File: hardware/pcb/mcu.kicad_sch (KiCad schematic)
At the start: 10 parts, among them J3 FSR402, U1 ESP32-WROOM-32E-N8R2

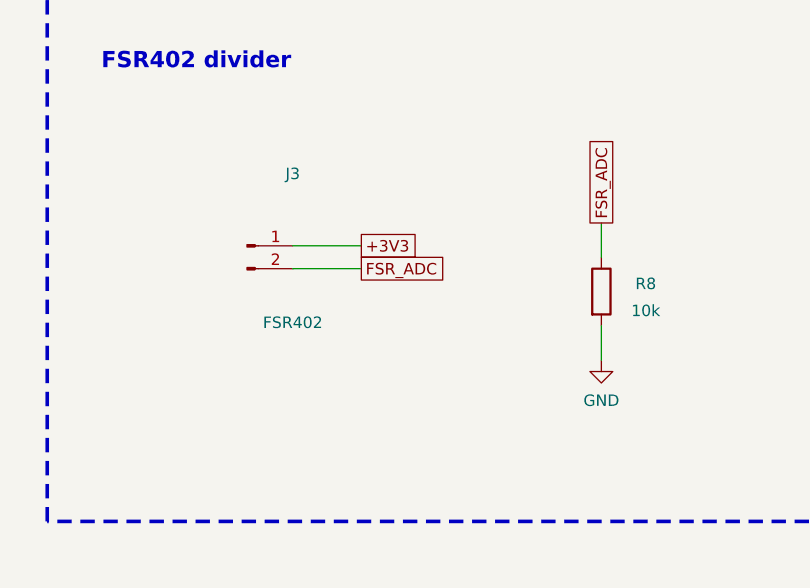
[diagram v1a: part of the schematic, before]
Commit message: Use official CAD and shrink the hw_v1 board to 37x30 mm.
Replace the hand-drawn AFE4900, AD5940, ADS1292R, AS7341, MLX90632,
TMP117, LSM6DSV80X, and MCP73831 symbols and footprints with the
SnapMagic and Ultra Librarian libraries. ADS1292R is now the QFN-32
ADS1292RIRSMT, and MLX90632SLD-DCB-100-SP moves SDA/SCL onto the
existing 1.8 V bus. Pin headers and mounting holes are flat solder
pads. The unrouted 4-layer placement keeps the antenna on the left
edge and the skin sensors together on the bottom.

Co-authored-by: Riyu-D1 <Riyu-D1@users.noreply.github.com>
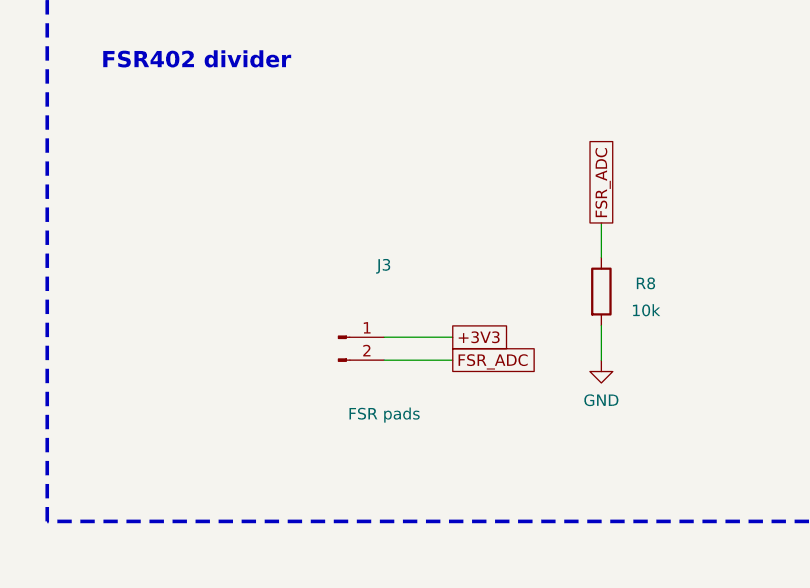
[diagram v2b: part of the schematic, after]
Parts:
- J3: value FSR402 -> FSR pads; footprint Connector_PinHeader_2.54mm:PinHeader_1x02_P2.54mm_Vertical -> vitalq:Pads_FSR
- TP1, TP2: now left out of the parts list

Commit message: Seat the QFN models and drop passives the datasheets do not require.
The ADS1292R STEP is already Z-up, so the extra X rotation stood the
4x4x1 mm body on edge. Remove TP1, TP2, C5, C12, C17, C31 and R4, add
the 1 uF AVDD bulk capacitor, and shorten the outline to 36.2 x 27.8 mm.

Co-authored-by: Riyu-D1 <Riyu-D1@users.noreply.github.com>
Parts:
- removed TP1: EN, TestPoint:TestPoint_Pad_D1.5mm, symbol vitalq:TestPoint
- removed TP2: IO0, TestPoint:TestPoint_Pad_D1.5mm, symbol vitalq:TestPoint
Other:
- note added: "EN and IO0 have pull-ups only. Download uses the module pads. There are no buttons."
- note removed: "TP1 and TP2 are pads so EN and IO0 can be strapped for download. There are no buttons."
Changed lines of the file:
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@@
 		(instances
 			(project "vitalq_hw_v1"
-				(path "/6fcf6b13-4a8e-4f25-a8b9-d34cb547168d/a5fd4a7f-7072-43f1-b967-7f2863112463"
+				(path "/1ff916b4-4a8a-459e-a757-b43de2b086a6/412652e5-da28-4ff8-bcda-4db89714720c"
 					(reference "U1")
 					(unit 1)
@@
 		(on_board no)
 		(dnp no)
-		(property "Reference" "#PWR028"
+		(property "Reference" "#PWR026"
 			(at 149.86 95.99 0)
 			(effects (font (size 1.27 1.27)) (hide yes))
@@
 		(instances
 			(project "vitalq_hw_v1"
-				(path "/6fcf6b13-4a8e-4f25-a8b9-d34cb547168d/a5fd4a7f-7072-43f1-b967-7f2863112463"
-					(reference "#PWR028")
+				(path "/1ff916b4-4a8a-459e-a757-b43de2b086a6/412652e5-da28-4ff8-bcda-4db89714720c"
+					(reference "#PWR026")
 					(unit 1)
 				)
@@
 		(on_board no)
 		(dnp no)
-		(property "Reference" "#PWR029"
+		(property "Reference" "#PWR027"
 			(at 149.86 179.81 0)
 			(effects (font (size 1.27 1.27)) (hide yes))
@@
 		(instances
 			(project "vitalq_hw_v1"
-				(path "/6fcf6b13-4a8e-4f25-a8b9-d34cb547168d/a5fd4a7f-7072-43f1-b967-7f2863112463"
-					(reference "#PWR029")
+				(path "/1ff916b4-4a8a-459e-a757-b43de2b086a6/412652e5-da28-4ff8-bcda-4db89714720c"
+					(reference "#PWR027")
 					(unit 1)
 				)
@@
 		(instances
 			(project "vitalq_hw_v1"
-				(path "/6fcf6b13-4a8e-4f25-a8b9-d34cb547168d/a5fd4a7f-7072-43f1-b967-7f2863112463"
+				(path "/1ff916b4-4a8a-459e-a757-b43de2b086a6/412652e5-da28-4ff8-bcda-4db89714720c"
 					(reference "C7")
 					(unit 1)
@@
 		(on_board no)
 		(dnp no)
-		(property "Reference" "#PWR030"
+		(property "Reference" "#PWR028"
 			(at 54.61 49.0 0)
 			(effects (font (size 1.27 1.27)) (hide yes))
@@
 		(instances
 			(project "vitalq_hw_v1"
-				(path "/6fcf6b13-4a8e-4f25-a8b9-d34cb547168d/a5fd4a7f-7072-43f1-b967-7f2863112463"
-					(reference "#PWR030")
+				(path "/1ff916b4-4a8a-459e-a757-b43de2b086a6/412652e5-da28-4ff8-bcda-4db89714720c"
+					(reference "#PWR028")
 					(unit 1)
 				)
@@
 		(on_board no)
 		(dnp no)
-		(property "Reference" "#PWR031"
+		(property "Reference" "#PWR029"
 			(at 54.61 64.24 0)
 			(effects (font (size 1.27 1.27)) (hide yes))
@@
 		(instances
 			(project "vitalq_hw_v1"
-				(path "/6fcf6b13-4a8e-4f25-a8b9-d34cb547168d/a5fd4a7f-7072-43f1-b967-7f2863112463"
-					(reference "#PWR031")
+				(path "/1ff916b4-4a8a-459e-a757-b43de2b086a6/412652e5-da28-4ff8-bcda-4db89714720c"
+					(reference "#PWR029")
 					(unit 1)
 				)
@@
 		(instances
 			(project "vitalq_hw_v1"
-				(path "/6fcf6b13-4a8e-4f25-a8b9-d34cb547168d/a5fd4a7f-7072-43f1-b967-7f2863112463"
+				(path "/1ff916b4-4a8a-459e-a757-b43de2b086a6/412652e5-da28-4ff8-bcda-4db89714720c"
 					(reference "C8")
 					(unit 1)
@@
 		(on_board no)
 		(dnp no)
-		(property "Reference" "#PWR032"
+		(property "Reference" "#PWR030"
 			(at 77.47 49.0 0)
 			(effects (font (size 1.27 1.27)) (hide yes))
@@
 		(instances
 			(project "vitalq_hw_v1"
-				(path "/6fcf6b13-4a8e-4f25-a8b9-d34cb547168d/a5fd4a7f-7072-43f1-b967-7f2863112463"
-					(reference "#PWR032")
+				(path "/1ff916b4-4a8a-459e-a757-b43de2b086a6/412652e5-da28-4ff8-bcda-4db89714720c"
+					(reference "#PWR030")
 					(unit 1)
 				)
@@
 		(on_board no)
 		(dnp no)
-		(property "Reference" "#PWR033"
+		(property "Reference" "#PWR031"
 			(at 77.47 64.24 0)
 			(effects (font (size 1.27 1.27)) (hide yes))
@@
 		(instances
 			(project "vitalq_hw_v1"
-				(path "/6fcf6b13-4a8e-4f25-a8b9-d34cb547168d/a5fd4a7f-7072-43f1-b967-7f2863112463"
-					(reference "#PWR033")
+				(path "/1ff916b4-4a8a-459e-a757-b43de2b086a6/412652e5-da28-4ff8-bcda-4db89714720c"
+					(reference "#PWR031")
 					(unit 1)
 				)
@@
 		(instances
 			(project "vitalq_hw_v1"
-				(path "/6fcf6b13-4a8e-4f25-a8b9-d34cb547168d/a5fd4a7f-7072-43f1-b967-7f2863112463"
+				(path "/1ff916b4-4a8a-459e-a757-b43de2b086a6/412652e5-da28-4ff8-bcda-4db89714720c"
 					(reference "R5")
 					(unit 1)
@@
 		(on_board no)
 		(dnp no)
-		(property "Reference" "#PWR034"
+		(property "Reference" "#PWR032"
 			(at 330.2 52.81 0)
 			(effects (font (size 1.27 1.27)) (hide yes))
@@
 		(instances
 			(project "vitalq_hw_v1"
-				(path "/6fcf6b13-4a8e-4f25-a8b9-d34cb547168d/a5fd4a7f-7072-43f1-b967-7f2863112463"
-					(reference "#PWR034")
+				(path "/1ff916b4-4a8a-459e-a757-b43de2b086a6/412652e5-da28-4ff8-bcda-4db89714720c"
+					(reference "#PWR032")
 					(unit 1)
 				)
@@
 		(instances
 			(project "vitalq_hw_v1"
-				(path "/6fcf6b13-4a8e-4f25-a8b9-d34cb547168d/a5fd4a7f-7072-43f1-b967-7f2863112463"
+				(path "/1ff916b4-4a8a-459e-a757-b43de2b086a6/412652e5-da28-4ff8-bcda-4db89714720c"
 					(reference "R6")
 					(unit 1)
@@
 		(on_board no)
 		(dnp no)
-		(property "Reference" "#PWR035"
+		(property "Reference" "#PWR033"
 			(at 351.79 52.81 0)
 			(effects (font (size 1.27 1.27)) (hide yes))
@@
 		(instances
 			(project "vitalq_hw_v1"
-				(path "/6fcf6b13-4a8e-4f25-a8b9-d34cb547168d/a5fd4a7f-7072-43f1-b967-7f2863112463"
-					(reference "#PWR035")
+				(path "/1ff916b4-4a8a-459e-a757-b43de2b086a6/412652e5-da28-4ff8-bcda-4db89714720c"
+					(reference "#PWR033")
 					(unit 1)
 				)
@@
 		(instances
 			(project "vitalq_hw_v1"
-				(path "/6fcf6b13-4a8e-4f25-a8b9-d34cb547168d/a5fd4a7f-7072-43f1-b967-7f2863112463"
+				(path "/1ff916b4-4a8a-459e-a757-b43de2b086a6/412652e5-da28-4ff8-bcda-4db89714720c"
 					(reference "R7")
 					(unit 1)
@@
 		(on_board no)
 		(dnp no)
-		(property "Reference" "#PWR036"
+		(property "Reference" "#PWR034"
 			(at 373.38 52.81 0)
 			(effects (font (size 1.27 1.27)) (hide yes))
@@
 		(instances
 			(project "vitalq_hw_v1"
-				(path "/6fcf6b13-4a8e-4f25-a8b9-d34cb547168d/a5fd4a7f-7072-43f1-b967-7f2863112463"
-					(reference "#PWR036")
-					(unit 1)
-				)
-			)
-		)
-	)
-	(symbol
-		(lib_id "vitalq:TestPoint")
-		(at 330.2 77.47 0)
-		(unit 1)
-		(exclude_from_sim no)
-		(in_bom no)
-		(on_board yes)
-		(dnp no)
-		(property "Reference" "TP1"
-			(at 334.5 76.6 0)
-			(effects (font (size 1.27 1.27)))
-		)
-		(property "Value" "EN"
-			(at 334.5 79.6 0)
-			(effects (font (size 1.27 1.27)))
-		)
-		(property "Footprint" "TestPoint:TestPoint_Pad_D1.5mm"
-			(at 330.2 77.47 0)
-			(effects (font (size 1.27 1.27)) (hide yes))
-		)
-		(property "Datasheet" ""
-			(at 330.2 77.47 0)
-			(effects (font (size 1.27 1.27)) (hide yes))
-		)
-		(pin "1")
-		(instances
-			(project "vitalq_hw_v1"
-				(path "/6fcf6b13-4a8e-4f25-a8b9-d34cb547168d/a5fd4a7f-7072-43f1-b967-7f2863112463"
-					(reference "TP1")
-					(unit 1)
-				)
-			)
-		)
-	)
-	(symbol
-		(lib_id "vitalq:TestPoint")
-		(at 359.41 77.47 0)
-		(unit 1)
-		(exclude_from_sim no)
-		(in_bom no)
-		(on_board yes)
-		(dnp no)
-		(property "Reference" "TP2"
-			(at 364.5 76.6 0)
-			(effects (font (size 1.27 1.27)))
-		)
-		(property "Value" "IO0"
-			(at 364.5 79.6 0)
-			(effects (font (size 1.27 1.27)))
-		)
-		(property "Footprint" "TestPoint:TestPoint_Pad_D1.5mm"
-			(at 359.41 77.47 0)
-			(effects (font (size 1.27 1.27)) (hide yes))
-		)
-		(property "Datasheet" ""
-			(at 359.41 77.47 0)
-			(effects (font (size 1.27 1.27)) (hide yes))
-		)
-		(pin "1")
-		(instances
-			(project "vitalq_hw_v1"
-				(path "/6fcf6b13-4a8e-4f25-a8b9-d34cb547168d/a5fd4a7f-7072-43f1-b967-7f2863112463"
-					(reference "TP2")
+				(path "/1ff916b4-4a8a-459e-a757-b43de2b086a6/412652e5-da28-4ff8-bcda-4db89714720c"
+					(reference "#PWR034")
 					(unit 1)
 				)
@@
 		(instances
 			(project "vitalq_hw_v1"
-				(path "/6fcf6b13-4a8e-4f25-a8b9-d34cb547168d/a5fd4a7f-7072-43f1-b967-7f2863112463"
+				(path "/1ff916b4-4a8a-459e-a757-b43de2b086a6/412652e5-da28-4ff8-bcda-4db89714720c"
 					(reference "J3")
 					(unit 1)
@@
 		(instances
 			(project "vitalq_hw_v1"
-				(path "/6fcf6b13-4a8e-4f25-a8b9-d34cb547168d/a5fd4a7f-7072-43f1-b967-7f2863112463"
+				(path "/1ff916b4-4a8a-459e-a757-b43de2b086a6/412652e5-da28-4ff8-bcda-4db89714720c"
 					(reference "R8")
 					(unit 1)
@@
 		(on_board no)
 		(dnp no)
-		(property "Reference" "#PWR037"
+		(property "Reference" "#PWR035"
 			(at 369.57 130.28 0)
 			(effects (font (size 1.27 1.27)) (hide yes))
@@
 		(instances
 			(project "vitalq_hw_v1"
-				(path "/6fcf6b13-4a8e-4f25-a8b9-d34cb547168d/a5fd4a7f-7072-43f1-b967-7f2863112463"
-					(reference "#PWR037")
+				(path "/1ff916b4-4a8a-459e-a757-b43de2b086a6/412652e5-da28-4ff8-bcda-4db89714720c"
+					(reference "#PWR035")
 					(unit 1)
 				)
@@
 		)
 	)
-	(wire
-		(pts
-			(xy 335.28 77.47)
-			(xy 340.36 77.47)
-		)
-		(stroke (width 0) (type default))
-	)
-	(global_label "ESP_EN"
-		(shape passive)
-		(at 340.36 77.47 0)
-		(effects (font (size 1.27 1.27)) (justify left))
-		(property "Intersheetrefs" "${INTERSHEET_REFS}"
-			(at 340.36 77.47 0)
-			(effects (font (size 1.27 1.27)) (hide yes))
-		)
-	)
-	(wire
-		(pts
-			(xy 364.49 77.47)
-			(xy 369.57 77.47)
-		)
-		(stroke (width 0) (type default))
-	)
-	(global_label "ESP_IO0"
-		(shape passive)
-		(at 369.57 77.47 0)
-		(effects (font (size 1.27 1.27)) (justify left))
-		(property "Intersheetrefs" "${INTERSHEET_REFS}"
-			(at 369.57 77.47 0)
-			(effects (font (size 1.27 1.27)) (hide yes))
-		)
-	)
 	(text "FSR402 divider"
 		(exclude_from_sim no)
@@
 		(effects (font (size 1.4 1.4)) (justify left bottom))
 	)
-	(text "TP1 and TP2 are pads so EN and IO0 can be strapped for download. There are no buttons."
+	(text "EN and IO0 have pull-ups only. Download uses the module pads. There are no buttons."
 		(exclude_from_sim no)
 		(at 16.0 216.0 0)

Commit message: Add the chest-board sensors and replace the 3.3 V LDO with a TPS63802.
The unrouted 40 x 34 mm board keeps every previous part except the off-board PPG pads, which the SFH 7072 replaces. Respiration, a second ECG lead, electrode protection, EDA, fuel gauge, flash, and the I/O expander are in the schematic.

Co-authored-by: Riyu-D1 <Riyu-D1@users.noreply.github.com>
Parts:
- added C59, C60: 100n, Capacitor_SMD:C_0402_1005Metric, symbol vitalq:C
- added R52, R53: 10k, Resistor_SMD:R_0402_1005Metric, symbol vitalq:R
- added U18: W25Q512JVEIQ, vitalq:W25Q512_WSON8, symbol vitalq:W25Q512JVEIQ
- added U19: TCA6408ARSVR, vitalq:TCA6408A_RSV, symbol vitalq:TCA6408ARSV
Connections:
- net +3V3: now also C59.1, C60.1, R52.1, R53.1, U18.3 (~{WP}/IO_{2}), U18.7 (~{HOLD}/~{RESET}/IO_{3}), U18.8 (VCC), U19.1 (~{RESET}), U19.14 (V_{CCP}), U19.15 (V_{CCI})
- net AD5940_RESET: now also U19.4 (P2); no longer U1.12 (IO27)
- net ADS1292_PWDN: now also U19.3 (P1); no longer U1.10 (IO25)
- net AFE4900_RESETZ: now also U19.2 (P0); no longer U1.28 (IO17)
- net GND: now also C59.2, C60.2, U18.4 (GND), U18.9 (EP), U19.16 (ADDR), U19.6 (GND)
- net I2C_SCL: now also U19.12 (SCL)
- net I2C_SDA: now also U19.13 (SDA)
- net SPI_MISO: now also U18.2 (DO/IO_{1})
- net SPI_MOSI: now also U18.5 (DI/IO_{0})
- net SPI_SCK: now also U18.6 (CLK)
- net EXP_INT: now reaches U1.7 (IO35)
- net EXP_INT: now also R53.2, U19.11 (~{INT})
- net ADS1292_START renamed CS_FLASH
- net CS_FLASH: now also R52.2, U18.1 (~{CS})
- new net CHG_STAT: U19.8 (P5)
- new net IR_GATE: U19.7 (P4)
- new net TX5_EN: U19.5 (P3)
- new net VBUS_DET: U19.9 (P6)
- no-connect marks 4 -> 7

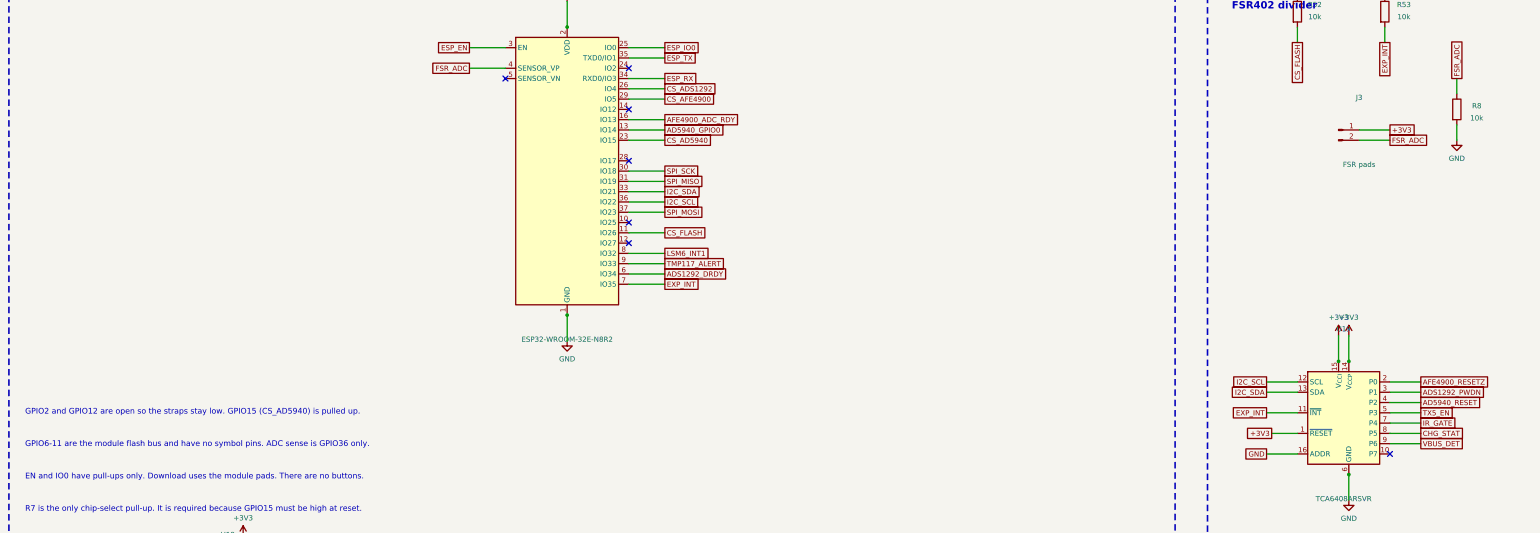
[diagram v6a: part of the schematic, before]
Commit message: Add defibrillator clamps and a charge-temperature cut-off.
Series electrode resistors are now DPCR2512 51k pulse parts, with an S30-A90X gas discharge tube on each patient pad ahead of the existing TPD1E10B06. The MCP73831 stays; a PicoStar FET floats PROG until firmware enables charge, and a 3-pin cell pad feeds a 10k NTC into GPIO39.

Co-authored-by: Riyu-D1 <Riyu-D1@users.noreply.github.com>
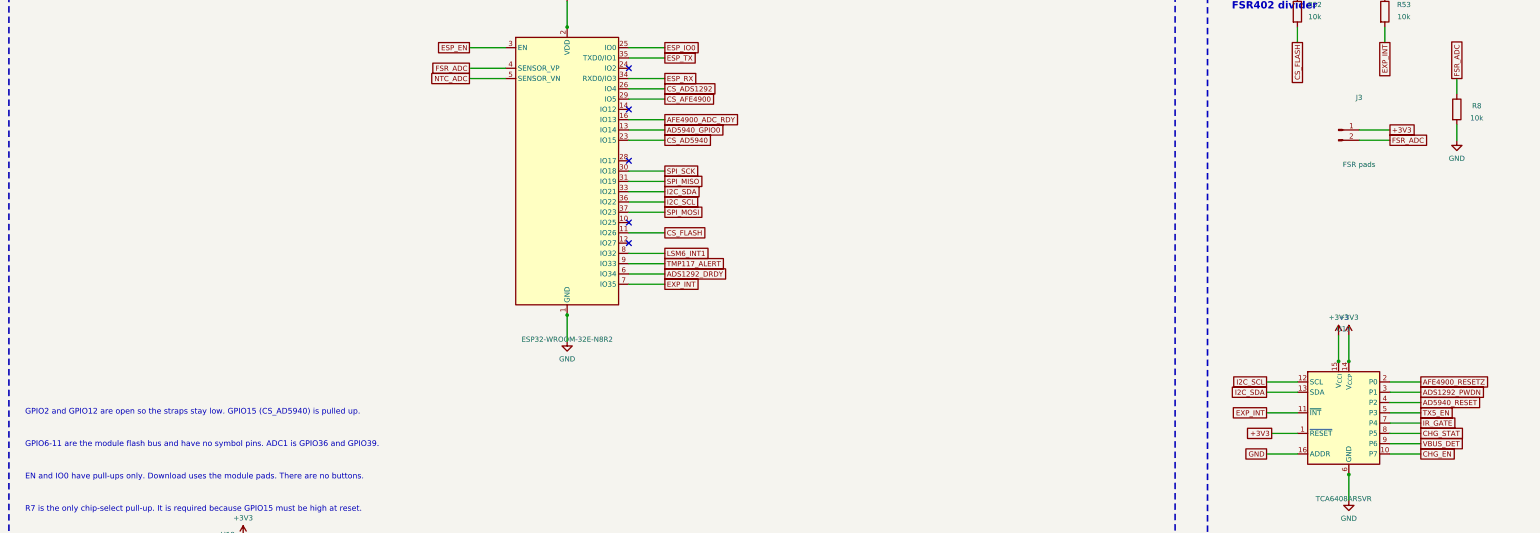
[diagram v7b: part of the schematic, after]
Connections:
- net NTC_ADC: now reaches U1.5 (SENSOR_VN)
- net CHG_EN: now reaches U19.10 (P7)
- no-connect marks 7 -> 5
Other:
- note added: "GPIO6-11 are the module flash bus and have no symbol pins. ADC1 is GPIO36 and GPIO39."
- note removed: "GPIO6-11 are the module flash bus and have no symbol pins. ADC sense is GPIO36 only."
